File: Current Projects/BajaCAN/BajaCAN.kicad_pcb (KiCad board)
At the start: 2 copper layers, 65.5 x 71.6 mm, 50 parts, among them J1 348300801, J2 ICSP, J3 348302004, J4 348302001, U1 AVR128DB32x-xRXB, U2 MCP1603, U3 MCP251863T-H-SS, Y1 OV-7604-C7, Y2 CSTNE20M0V530000R0

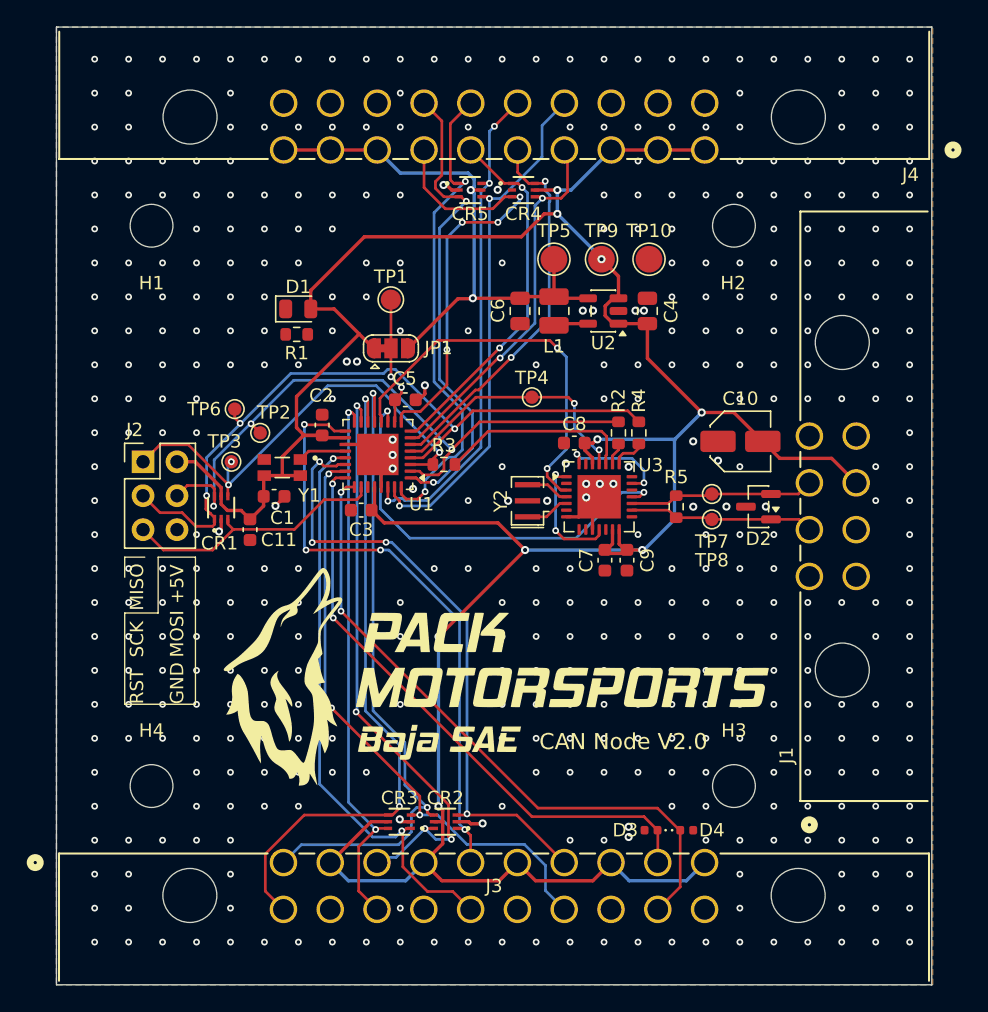
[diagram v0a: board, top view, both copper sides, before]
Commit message: Slightly moved back silkscreen and added connector labels
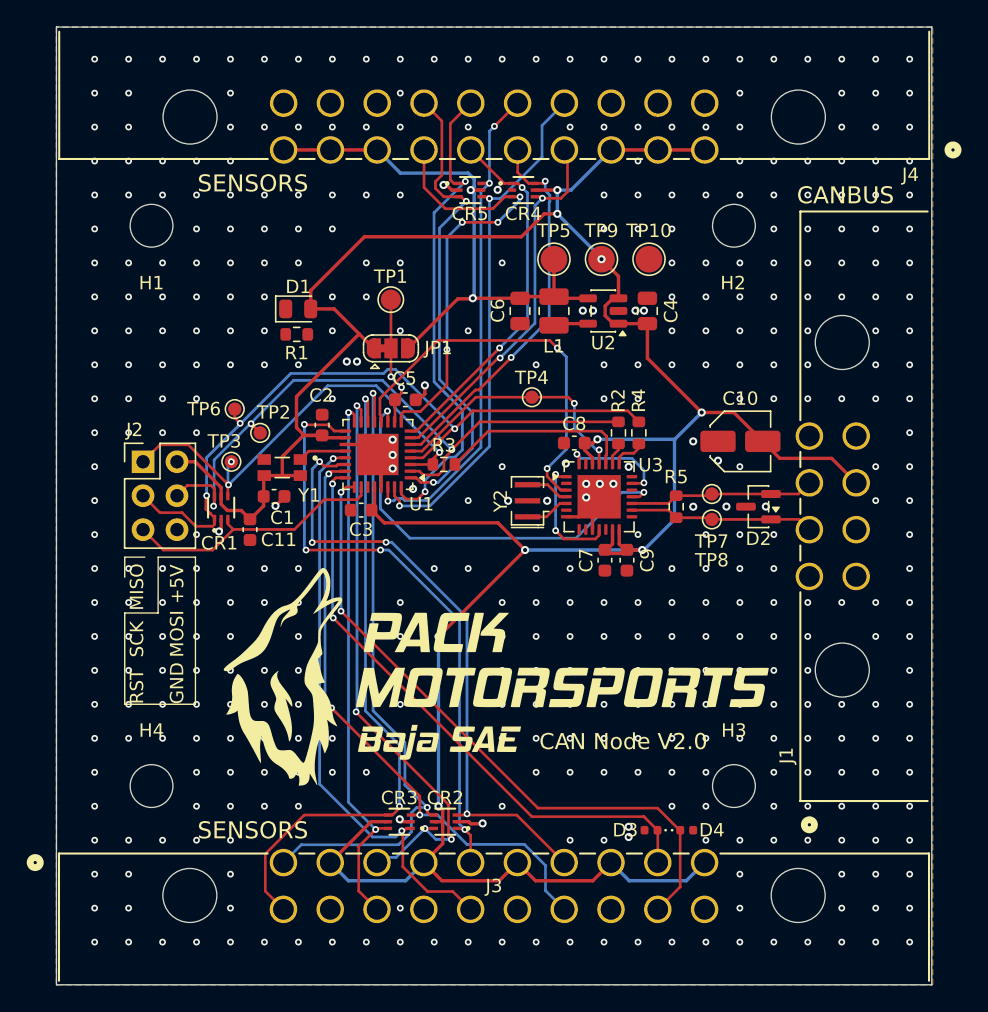
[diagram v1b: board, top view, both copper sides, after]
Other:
- board text added: "CANBUS"
- board text added: "SENSORS"
